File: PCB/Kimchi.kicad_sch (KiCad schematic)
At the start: 1 part, among them SW1 SW_MEC_5E

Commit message: WIP PCB
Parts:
- added B1neg1, B1pos1, B2neg1, B2pos1, B4b1, BJMP1gnd1, BJMP1neg1, BJMP2neg1: TestPoint, TestPoint:TestPoint_Pad_D2.0mm, symbol Connector:TestPoint
- added C1, C2, C3: C, Capacitor_SMD:C_0603_1608Metric, symbol Device:C
- added H1, H2, H3, H4, H5, H6, H7, H8: MountingHole, MountingHole:MountingHole_2.2mm_M2_DIN965, symbol Mechanical:MountingHole
- added LD1, LD2, LD3: ~, matseng:OSK2028A, symbol matseng:7SEG-2-CC
- added RN1, RN2: R_Pack04, Resistor_SMD:R_Array_Convex_4x0603, symbol Device:R_Pack04
- added SW0, SW2, SW22, SW23, SW3, SW4, SW5, SW6, SW7, SW8, SW9, SWa1, SWad1, SWb1, SWc1, SWd1, SWda1, SWe1, SWf1, SWgo1, SWpc1, SWplus1: SW_MEC_5E, matseng:TVCU18, symbol Switch:SW_MEC_5E
- added SW24, SW25: SW_SPDT, Button_Switch_SMD:SW_SPDT_PCM12, symbol Switch:SW_SPDT
- added U1: 7442, Package_SO:SOIC-16_3.9x9.9mm_P1.27mm, symbol 74xx_IEEE:7442
- added U2: HT75xx-1-SOT89, Package_TO_SOT_SMD:SOT-89-3, symbol Regulator_Linear:HT75xx-1-SOT89
- added U3: ~, Package_SO:SSOP-20_4.4x6.5mm_P0.65mm, symbol matseng:CH32V003F4P6
- SW1: footprint Button_Switch_SMD:SW_SPST_PTS645 -> matseng:TVCU18
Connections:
- net COLf: now reaches SW1.1
- net COLf: now also SW1.2, RN2.6 (R3.2), SW8.1, SW8.2, SWf1.1, SWf1.2, U3.15 (PC5)
- net ROW0: now reaches SW1.3 (K)
- net ROW0: now also SW1.4 (A), SW0.3 (K), SW0.4 (A), SW2.3 (K), SW2.4 (A), SW3.3 (K), SW3.4 (A), SW4.3 (K), SW4.4 (A), SW5.3 (K), SW5.4 (A), SW6.3 (K), SW6.4 (A), U1.1 (~{Q0})
- new net: B1pos1.1, BJMP2neg1.1
- new net: LD1.3 (A), LD2.3 (A), LD3.3 (A), RN2.1 (R1.1)
- new net: LD1.1 (G), LD2.1 (G), LD3.1 (G), RN2.2 (R2.1)
- new net: LD1.4 (F), LD2.4 (F), LD3.4 (F), RN2.3 (R3.1)
- new net: LD1.7 (E), LD2.7 (E), LD3.7 (E), RN2.4 (R4.1)
- new net: B2pos1.1, SW25.2 (B)
- new net: C1.1, SW25.1 (A), U2.2 (VIN)
- new net: LD1.6 (D), LD2.6 (D), LD3.6 (D), RN1.1 (R1.1)
- new net: LD1.8 (C), LD2.8 (C), LD3.8 (C), RN1.2 (R2.1)
- new net: LD1.9 (B), LD2.9 (B), LD3.9 (B), RN1.3 (R3.1)
- new net: SW22.1, SW22.2, U3.6 (PA2)
- new net: LD2.10 (DIG1), U1.7 (~{Q6})
- new net: LD2.5 (DIG2), U1.9 (~{Q7})
- new net: LD3.10 (DIG1), U1.10 (~{Q8})
- new net: LD3.5 (DIG2), U1.11 (~{Q9})
- new net: LD1.10 (DIG1), U1.5 (~{Q4})
- new net: LD1.5 (DIG2), U1.6 (~{Q5})
- new net: SW24.2 (B), U3.4 (PD7)
- new net: B2neg1.1, B4b1.1
- new net: U1.12 (A3), U3.3 (PD6)
- new net: U1.13 (A2), U3.2 (PD5)
- new net: U1.14 (A1), U3.1 (PD4)
- new net: U1.15 (A0), U3.20 (PD3)
- new net: SW23.1, SW23.2, U3.5 (PA1)
- new net: B1neg1.1, BJMP1neg1.1
- new net +5V: C2.1, C3.1, U1.16 (VCC), U2.3 (VOUT), U3.9 (VDD)
- new net COLa: RN2.8 (R1.2), SW6.1, SW6.2, SWd1.1, SWd1.2, SWgo1.1, SWgo1.2, U3.10 (PC0)
- new net COLb: RN1.6 (R3.2), SW5.1, SW5.2, SWc1.1, SWc1.2, SWplus1.1, SWplus1.2, U3.11 (PC1)
- new net COLc: RN1.7 (R2.2), SW4.1, SW4.2, SWb1.1, SWb1.2, SWpc1.1, SWpc1.2, U3.12 (PC2)
- new net COLd: RN1.8 (R1.2), SW3.1, SW3.2, SWa1.1, SWa1.2, SWda1.1, SWda1.2, U3.13 (PC3)
- new net COLe: RN2.5 (R4.2), SW2.1, SW2.2, SW9.1, SW9.2, SWad1.1, SWad1.2, U3.14 (PC4)
- new net COLg: RN2.7 (R2.2), SW0.1, SW0.2, SW7.1, SW7.2, SWe1.1, SWe1.2, U3.16 (PC6)
- new net GND: BJMP1gnd1.1, C1.2, C2.2, C3.2, SW22.3 (K), SW22.4 (A), SW23.3 (K), SW23.4 (A), SW24.3 (C), U1.8 (GND), U2.1 (GND), U3.7 (VSS)
- new net ROW1: SW7.3 (K), SW7.4 (A), SW8.3 (K), SW8.4 (A), SW9.3 (K), SW9.4 (A), SWa1.3 (K), SWa1.4 (A), SWb1.3 (K), SWb1.4 (A), SWc1.3 (K), SWc1.4 (A), SWd1.3 (K), SWd1.4 (A), U1.2 (~{Q1})
- new net ROW2: SWad1.3 (K), SWad1.4 (A), SWda1.3 (K), SWda1.4 (A), SWe1.3 (K), SWe1.4 (A), SWf1.3 (K), SWf1.4 (A), SWgo1.3 (K), SWgo1.4 (A), SWpc1.3 (K), SWpc1.4 (A), SWplus1.3 (K), SWplus1.4 (A), U1.3 (~{Q2})
- no-connect marks 0 -> 9
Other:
- title: (none) -> KIMICHI - KIM-1 Emulator based on CH32V003

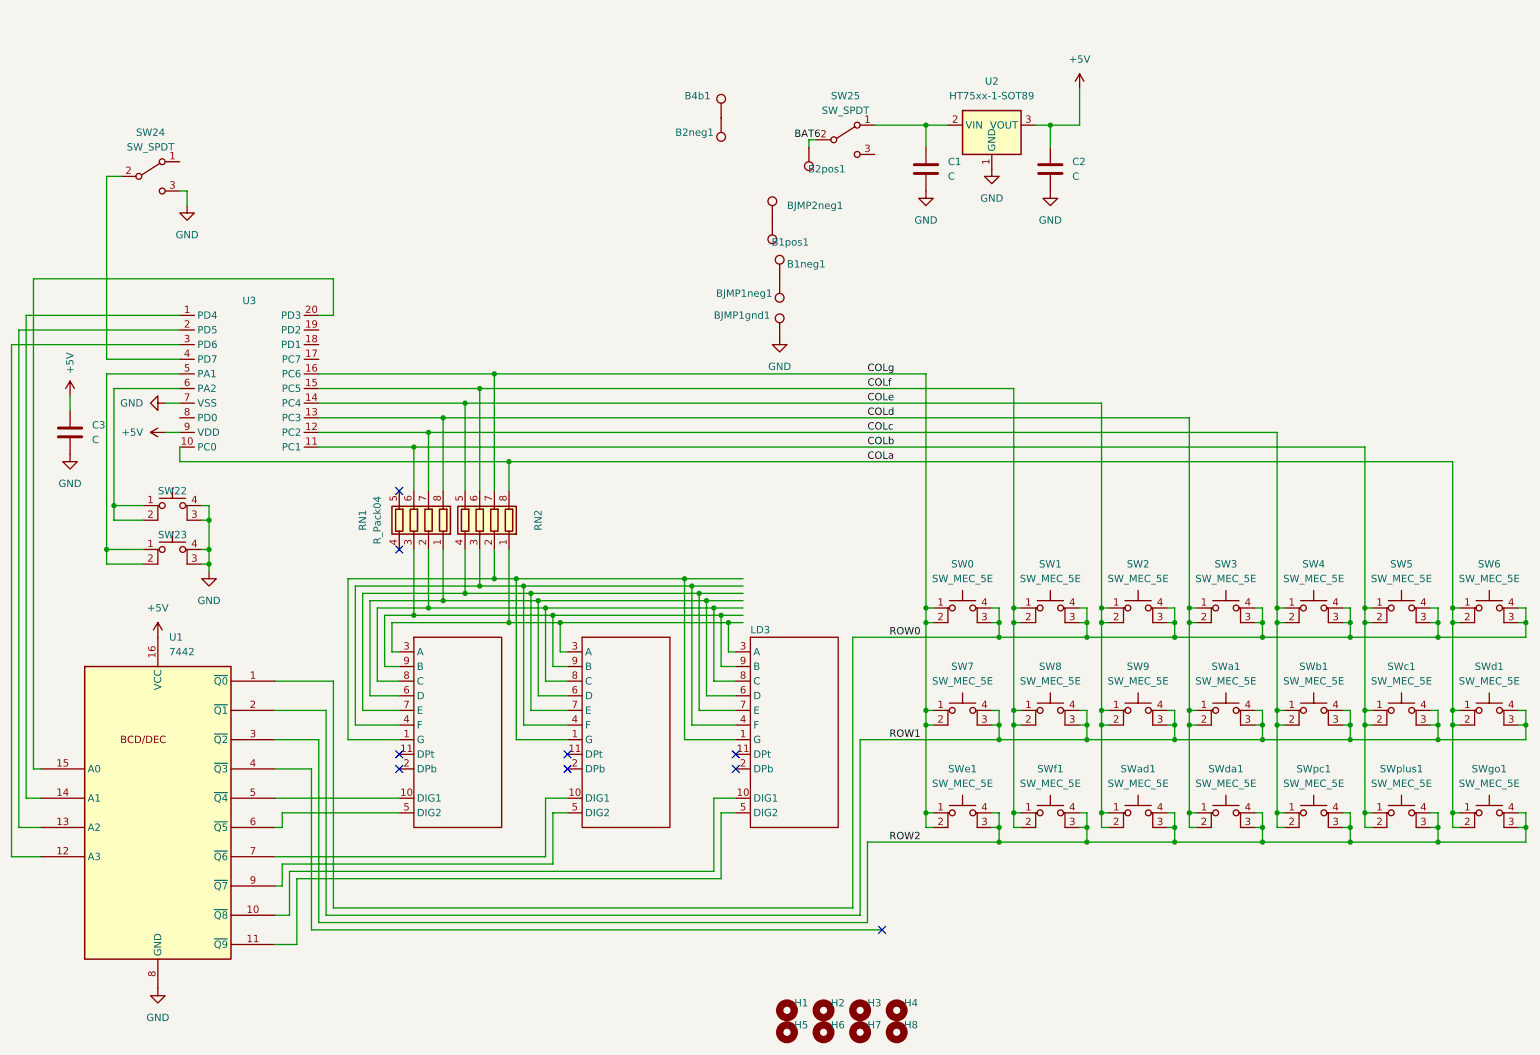
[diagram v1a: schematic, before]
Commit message: Trying to balance copper
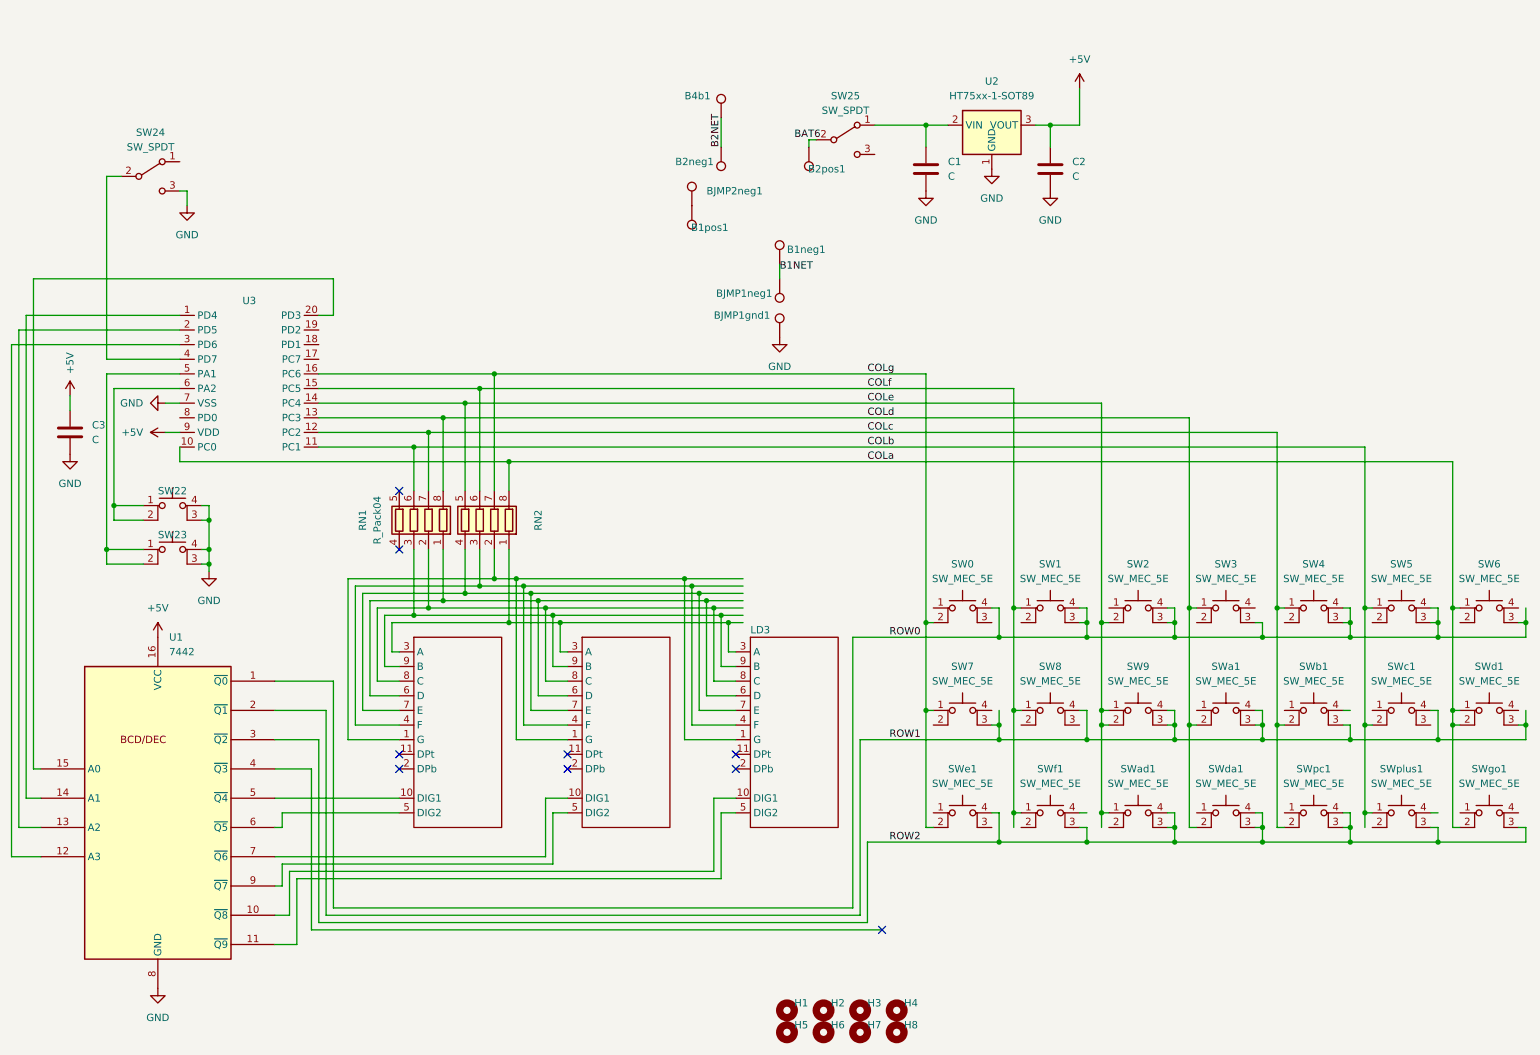
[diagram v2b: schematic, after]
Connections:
- net COLa: no longer SW6.2, SWgo1.1
- net COLb: no longer SW5.2, SWc1.1, SWplus1.2
- net COLc: no longer SW4.2, SWb1.1, SWpc1.1
- net COLd: no longer SW3.2, SWa1.1, SWda1.1
- net COLe: no longer SW2.1, SWad1.2
- net COLf: no longer SW1.2, SW8.2, SWf1.2
- net COLg: no longer SW0.1, SW7.2, SWe1.1
- net ROW0: no longer SW0.3 (K), SW3.4 (A), SW6.4 (A)
- net ROW1: no longer SW7.4 (A), SW8.3 (K), SWb1.4 (A), SWc1.3 (K), SWd1.4 (A)
- net ROW2: no longer SWe1.3 (K), SWf1.4 (A), SWgo1.4 (A), SWplus1.4 (A)
- net B2NET: now reaches B2neg1.1, B4b1.1
- net B1NET: now reaches B1neg1.1, BJMP1neg1.1
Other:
- moved on the sheet: B1neg1, B1pos1, B2neg1, BJMP2neg1

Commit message: More WIP. Is now complex
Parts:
- removed B1neg1, B2neg1, B4b1, BJMP1neg1: TestPoint, TestPoint:TestPoint_Pad_D2.0mm, symbol Connector:TestPoint
- removed H1, H2, H3, H4, H5, H6, H7, H8: MountingHole, MountingHole:MountingHole_2.2mm_M2_DIN965, symbol Mechanical:MountingHole
- added B1neg1x1, B2neg1x1, B4b1x1, BJMP1neg1x1: TestPoint, TestPoint:TestPoint_Pad_D2.0mm, symbol Connector:TestPoint
- added H10, H12, H13, H14, H15, H16, H18, H20: MountingHole_Pad, MountingHole:MountingHole_2.2mm_M2_DIN965_Pad_TopBottom, symbol Mechanical:MountingHole_Pad
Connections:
- new net: B2neg1x1.1, B4b1x1.1, H12.1, H15.1, H16.1, H18.1
- new net: B1neg1x1.1, BJMP1neg1x1.1, H10.1, H13.1, H14.1, H20.1
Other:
- moved on the sheet: B1pos1, B2pos1, BJMP1gnd1, BJMP2neg1, C1, C2, SW25, U2

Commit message: Cleanups
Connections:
- net GND: now also B1neg1x1.1, BJMP1neg1x1.1, H10.1, H13.1, H14.1, H20.1
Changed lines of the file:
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@@
   (junction (at 265.43 123.19) (diameter 0) (color 0 0 0 0)
+  )
+  (junction (at 122.555 41.275) (diameter 0) (color 0 0 0 0)
   )
   (junction (at 90.17 120.65) (diameter 0) (color 0 0 0 0)
@@
     (stroke (width 0) (type default))
   )
+  (wire (pts (xy 122.555 41.275) (xy 127 41.275))
+    (stroke (width 0) (type default))
+  )
   (wire (pts (xy 142.24 128.27) (xy 143.51 128.27))
     (stroke (width 0) (type default))
@@
   )
   (wire (pts (xy 176.53 138.43) (xy 176.53 158.75))
+    (stroke (width 0) (type default))
+  )
+  (wire (pts (xy 127 41.275) (xy 127 50.165))
     (stroke (width 0) (type default))
   )
@@
         )
       )
+    )
+  )
+  (symbol (lib_id "power:GND") (at 127 50.165 0) (unit 1)
+    (in_bom yes) (on_board yes) (dnp no) (fields_autoplaced)
+    (property "Reference" "#PWR014" (at 127 56.515 0)
+      (effects (font (size 1.27 1.27)) hide)
+    )
+    (property "Value" "GND" (at 127 54.61 0)
+      (effects (font (size 1.27 1.27)))
+    )
+    (property "Footprint" "" (at 127 50.165 0)
+      (effects (font (size 1.27 1.27)) hide)
+    )
+    (property "Datasheet" "" (at 127 50.165 0)
+      (effects (font (size 1.27 1.27)) hide)
+    )
+    (pin "1")
+    (instances
+      (project "Kimchi"
+        (path "/24a12ebd-398d-453b-bf0d-fe545a334307"
+          (reference "#PWR014") (unit 1)
+        )
+      )

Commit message: Final verification
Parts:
- added TP1, TP2, TP3, TP4, TP5: TestPoint, TestPoint:TestPoint_THTPad_2.0x2.0mm_Drill1.0mm, symbol Connector:TestPoint
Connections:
- net +5V: now also TP3.1
- net GND: now also TP2.1
- net at B1pos1.1, BJMP2neg1.1: now also B2neg1x1.1, B4b1x1.1, H12.1, H15.1, H16.1, H18.1
- net at U3.18 (PD1): now also TP1.1
- no-connect marks 9 -> 11
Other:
- moved on the sheet: B1pos1, B2neg1x1, BJMP1gnd1, BJMP2neg1

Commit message: Rev0 sent to Aisler
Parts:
- added PD0, TTYgnd1, TTYin1, TTYout1: TestPoint, TestPoint:TestPoint_Pad_2.0x2.0mm, symbol Connector:TestPoint
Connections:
- net GND: now also TTYgnd1.1
- net at U3.17 (PC7): now also TTYin1.1
- net at U3.19 (PD2): now also TTYout1.1
- net at U3.8 (PD0): now also PD0.1
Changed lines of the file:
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@@
+    (stroke (width 0) (type default))
+  )
+  (wire (pts (xy 69.215 41.91) (xy 72.39 41.91))
     (stroke (width 0) (type default))
   )
@@
     (stroke (width 0) (type default))
   )
+  (wire (pts (xy 67.945 40.005) (xy 72.39 40.005))
+    (stroke (width 0) (type default))
+  )
   (wire (pts (xy 234.95 158.75) (xy 234.95 161.29))
     (stroke (width 0) (type default))
@@
     (stroke (width 0) (type default))
   )
+  (wire (pts (xy 71.12 77.47) (xy 76.835 77.47))
+    (stroke (width 0) (type default))
+  )
   (wire (pts (xy 122.555 31.75) (xy 122.555 35.56))
     (stroke (width 0) (type default))
@@
     (stroke (width 0) (type default))
   )
+  (wire (pts (xy 67.945 58.42) (xy 76.835 58.42))
+    (stroke (width 0) (type default))
+  )
   (wire (pts (xy 19.05 72.39) (xy 19.05 158.75))
     (stroke (width 0) (type default))
@@
     (stroke (width 0) (type default))
   )
+  (wire (pts (xy 67.945 40.005) (xy 67.945 58.42))
+    (stroke (width 0) (type default))
+  )
   (wire (pts (xy 222.25 120.65) (xy 222.25 140.97))
     (stroke (width 0) (type default))
@@
     (stroke (width 0) (type default))
   )
+  (wire (pts (xy 69.215 59.055) (xy 76.2 59.055))
+    (stroke (width 0) (type default))
+  )
   (wire (pts (xy 71.12 85.09) (xy 96.52 85.09))
     (stroke (width 0) (type default))
@@
     (stroke (width 0) (type default))
   )
+  (wire (pts (xy 45.72 87.63) (xy 46.99 87.63))
+    (stroke (width 0) (type default))
+  )
   (wire (pts (xy 90.17 90.17) (xy 237.49 90.17))
     (stroke (width 0) (type default))
@@
     (stroke (width 0) (type default))
   )
+  (wire (pts (xy 76.2 59.055) (xy 76.2 72.39))
+    (stroke (width 0) (type default))
+  )
   (wire (pts (xy 63.5 179.07) (xy 67.31 179.07))
     (stroke (width 0) (type default))
@@
     (stroke (width 0) (type default))
   )
+  (wire (pts (xy 76.835 58.42) (xy 76.835 77.47))
+    (stroke (width 0) (type default))
+  )
   (wire (pts (xy 267.97 138.43) (xy 269.24 138.43))
     (stroke (width 0) (type default))
@@
     (stroke (width 0) (type default))
   )
+  (wire (pts (xy 69.215 41.91) (xy 69.215 59.055))
+    (stroke (width 0) (type default))
+  )
   (wire (pts (xy 76.2 115.57) (xy 76.2 143.51))
     (stroke (width 0) (type default))
@@
     (stroke (width 0) (type default))
   )
+  (wire (pts (xy 71.12 72.39) (xy 76.2 72.39))
+    (stroke (width 0) (type default))
+  )
   (wire (pts (xy 46.99 92.71) (xy 46.99 95.25))
     (stroke (width 0) (type default))
@@
     (stroke (width 0) (type default))
   )
+  (wire (pts (xy 45.72 97.79) (xy 52.07 97.79))
+    (stroke (width 0) (type default))
+  )
   (wire (pts (xy 203.2 120.65) (xy 204.47 120.65))
     (stroke (width 0) (type default))
@@
   )
   (wire (pts (xy 71.12 82.55) (xy 99.06 82.55))
+    (stroke (width 0) (type default))
+  )
+  (wire (pts (xy 45.72 87.63) (xy 45.72 97.79))
     (stroke (width 0) (type default))
   )
@@
     (effects (font (size 1.27 1.27)) (justify left bottom))
   )
+  (symbol (lib_id "Connector:TestPoint") (at 72.39 41.91 270) (unit 1)
+    (in_bom yes) (on_board yes) (dnp no)
+    (property "Reference" "TTYout1" (at 76.2 41.91 90)
+      (effects (font (size 1.27 1.27)) (justify left))
+    )
+    (property "Value" "TestPoint" (at 78.74 41.91 90)
+      (effects (font (size 1.27 1.27)) (justify left))
+    )
+    (property "Footprint" "TestPoint:TestPoint_Pad_2.0x2.0mm" (at 72.39 46.99 0)
+      (effects (font (size 1.27 1.27)) hide)
+    )
+    (property "Datasheet" "~" (at 72.39 46.99 0)
+      (effects (font (size 1.27 1.27)) hide)
+    )
+    (pin "1")
+    (instances
+      (project "Kimchi"
+        (path "/24a12ebd-398d-453b-bf0d-fe545a334307"
+          (reference "TTYout1") (unit 1)
+        )
+      )
+    )
+  )
   (symbol (lib_id "Connector:TestPoint") (at 96.52 62.23 270) (unit 1)
     (in_bom yes) (on_board yes) (dnp no)
@@
         (path "/24a12ebd-398d-453b-bf0d-fe545a334307"
           (reference "#PWR03") (unit 1)
+        )
+      )
+    )
+  )
+  (symbol (lib_id "Connector:TestPoint") (at 72.39 40.005 270) (unit 1)
+    (in_bom yes) (on_board yes) (dnp no)
+    (property "Reference" "TTYin1" (at 76.2 40.005 90)
+      (effects (font (size 1.27 1.27)) (justify left))
+    )
+    (property "Value" "TestPoint" (at 78.74 40.005 90)
+      (effects (font (size 1.27 1.27)) (justify left))
+    )
+    (property "Footprint" "TestPoint:TestPoint_Pad_2.0x2.0mm" (at 72.39 45.085 0)
+      (effects (font (size 1.27 1.27)) hide)
+    )
+    (property "Datasheet" "~" (at 72.39 45.085 0)
+      (effects (font (size 1.27 1.27)) hide)
+    )
+    (pin "1")
+    (instances
+      (project "Kimchi"
+        (path "/24a12ebd-398d-453b-bf0d-fe545a334307"
+          (reference "TTYin1") (unit 1)
         )
       )
@@
     )
   )
+  (symbol (lib_id "power:GND") (at 72.39 44.45 0) (unit 1)
+    (in_bom yes) (on_board yes) (dnp no) (fields_autoplaced)
+    (property "Reference" "#PWR017" (at 72.39 50.8 0)
+      (effects (font (size 1.27 1.27)) hide)
+    )
+    (property "Value" "GND" (at 72.39 49.53 0)
+      (effects (font (size 1.27 1.27)))
+    )
+    (property "Footprint" "" (at 72.39 44.45 0)
+      (effects (font (size 1.27 1.27)) hide)
+    )
+    (property "Datasheet" "" (at 72.39 44.45 0)
+      (effects (font (size 1.27 1.27)) hide)
+    )
+    (pin "1")
+    (instances
+      (project "Kimchi"
+        (path "/24a12ebd-398d-453b-bf0d-fe545a334307"
+          (reference "#PWR017") (unit 1)
+        )
+      )
+    )
+  )
   (symbol (lib_id "Switch:SW_MEC_5E") (at 182.88 158.75 0) (unit 1)
     (in_bom yes) (on_board yes) (dnp no) (fields_autoplaced)
@@
         (path "/24a12ebd-398d-453b-bf0d-fe545a334307"
           (reference "SWe1") (unit 1)
+        )
+      )
+    )
+  )
+  (symbol (lib_id "Connector:TestPoint") (at 52.07 97.79 270) (unit 1)
+    (in_bom yes) (on_board yes) (dnp no)
+    (property "Reference" "PD0" (at 55.88 97.79 90)
+      (effects (font (size 1.27 1.27)) (justify left))
+    )
+    (property "Value" "TestPoint" (at 58.42 97.79 90)
+      (effects (font (size 1.27 1.27)) (justify left))
+    )
+    (property "Footprint" "TestPoint:TestPoint_Pad_2.0x2.0mm" (at 52.07 102.87 0)
+      (effects (font (size 1.27 1.27)) hide)
+    )
+    (property "Datasheet" "~" (at 52.07 102.87 0)
+      (effects (font (size 1.27 1.27)) hide)
+    )
+    (pin "1")
+    (instances
+      (project "Kimchi"
+        (path "/24a12ebd-398d-453b-bf0d-fe545a334307"
+          (reference "PD0") (unit 1)
         )
       )
@@
         )
       )
+    )
+  )
+  (symbol (lib_id "Connector:TestPoint") (at 72.39 44.45 270) (unit 1)
+    (in_bom yes) (on_board yes) (dnp no)
+    (property "Reference" "TTYgnd1" (at 76.2 44.45 90)
+      (effects (font (size 1.27 1.27)) (justify left))
+    )
+    (property "Value" "TestPoint" (at 78.74 44.45 90)
+      (effects (font (size 1.27 1.27)) (justify left))
+    )
+    (property "Footprint" "TestPoint:TestPoint_Pad_2.0x2.0mm" (at 72.39 49.53 0)
+      (effects (font (size 1.27 1.27)) hide)
+    )
+    (property "Datasheet" "~" (at 72.39 49.53 0)
+      (effects (font (size 1.27 1.27)) hide)
+    )
+    (pin "1")
+    (instances
+      (project "Kimchi"
+        (path "/24a12ebd-398d-453b-bf0d-fe545a334307"
+          (reference "TTYgnd1") (unit 1)
+        )
+      )
